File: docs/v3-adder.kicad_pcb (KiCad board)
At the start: 2 copper layers, 19.6 x 111.5 mm, 101 parts, among them J1 Thonkiconn, J2 Thonkiconn, J3 Thonkiconn, J4 Thonkiconn, J5 Thonkiconn, J6 Thonkiconn, J7 Thonkiconn, J8 Thonkiconn, P1 Eurorack 2x5, SW1 200-MSP3 (SPDT ON-OFF-ON), SW2 200-MSP3 (SPDT ON-OFF-ON), SW3 200-MSP3 (SPDT ON-OFF-ON), SW4 200-MSP3 (SPDT ON-OFF-ON), SW5 200-MSP1 (SPDT ON-ON), SW6 200-MDP6 (DPDT ON-ON-ON), SW7 200-MDP6 (DPDT ON-ON-ON), SW8 200-MDP6 (DPDT ON-ON-ON), U1 OPA4196, U2 OPA4196, U3 OPA4196, U4 L78L05, U5 L79L05

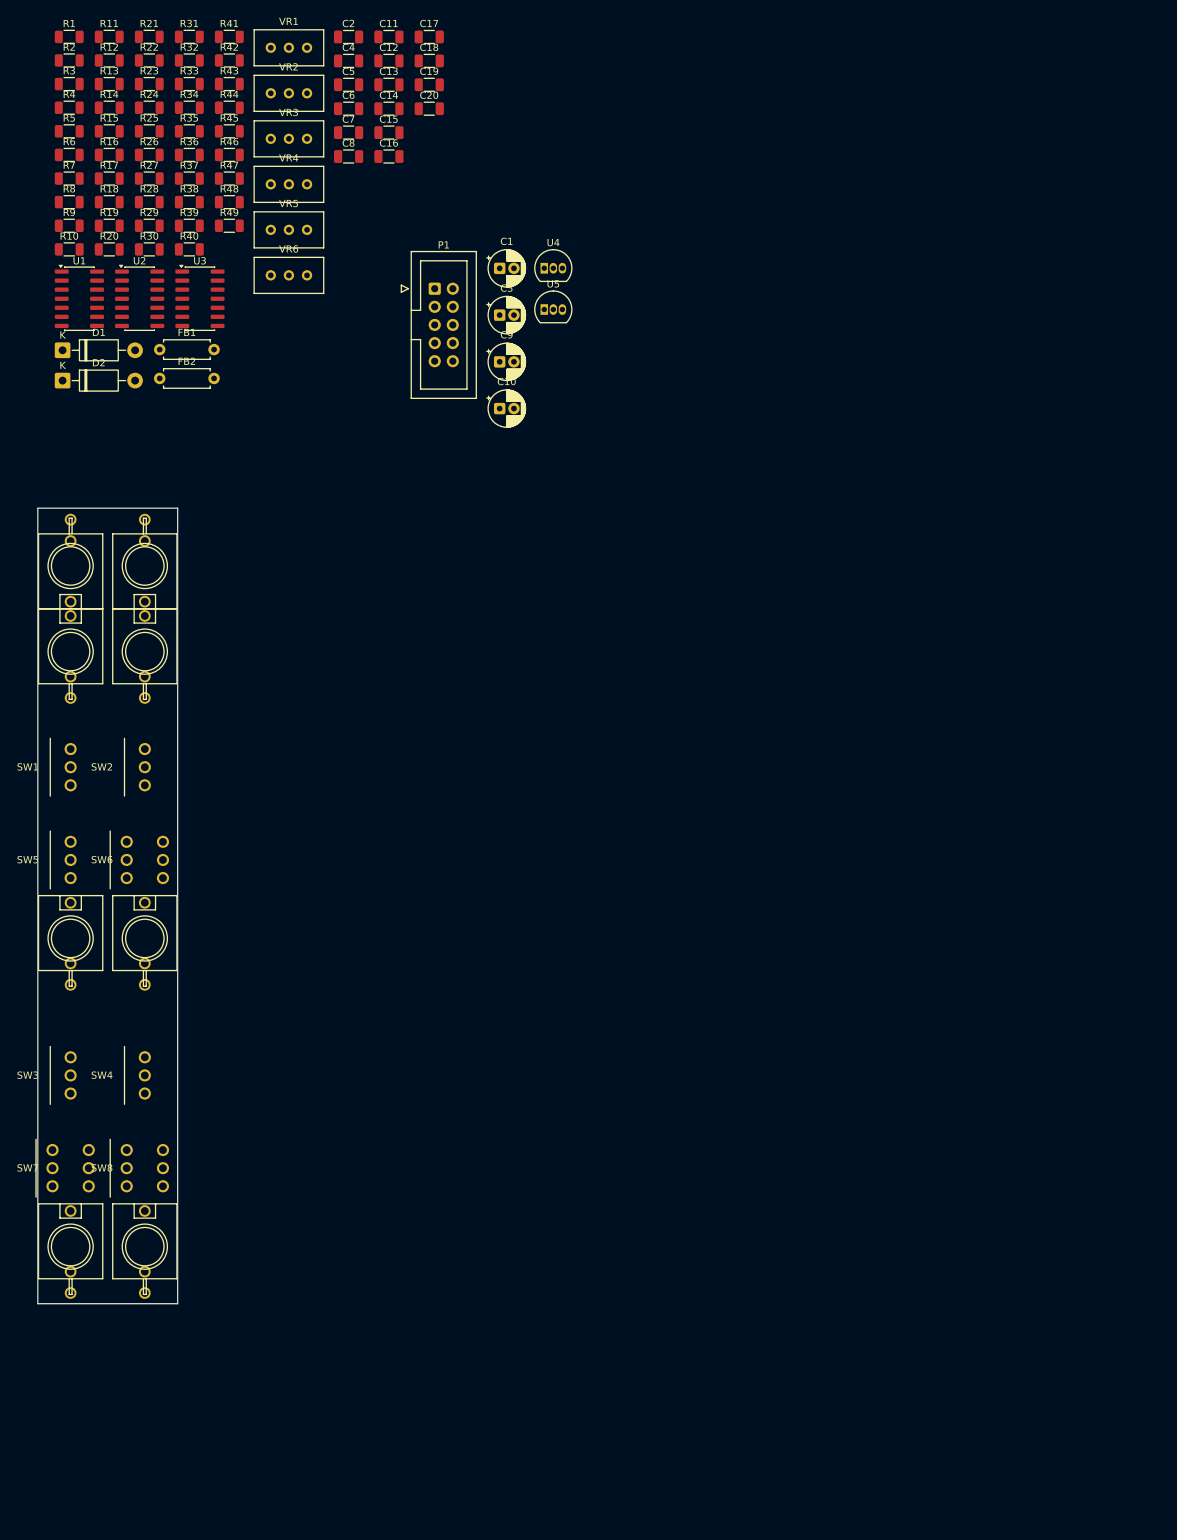
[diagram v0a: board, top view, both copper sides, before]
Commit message: Put component values on silk, and write them the same way in both files
Moves all 68 Fab-layer values to the matching silk layer, F.Fab -> F.SilkS
and B.Fab -> B.SilkS so back-side parts keep their mirrored justify. The 20
values that were already hidden stay hidden: "200-MDP6 (DPDT ON-ON-ON)" has
nowhere to go on a 19.6 mm board.

Trailing zeros that carry no information go with them -- 10.0k reads 10k,
1.00k reads 1k -- while 49.9k, 24.3k, 22.6k, 5.49k and 619R keep every
digit. Tolerance was never legible at 4 HP anyway; it lives in the BOM.

This turned out to be a consistency fix rather than a cosmetic one. The
schematic was the clean side: all ten 1k parts read 1.00k there and all
twenty 10k read 10.0k, but three of them had been edited to 1k in pcbnew,
and R8 disagreed outright (20.0k against the board's 20k). R31 read 1.00k
beside R32's 1k in the same ladder; R30 read 3.00k while R40, its exact
peer one stage along, read 3k. All 101 references now match between
schematic and board, with the netlist node-for-node identical to before
the edit and ERC still at zero.

gen_schematic.py moves in lockstep -- both the emitted values and the
check_function comparison strings, or --check would start failing. The E24
rationale comment keeps its decimals, since the argument turns on 3.01k
against 3.00k.

The BOM's "changes from what is currently in the schematic" table now reads
backwards for its first two rows, so it gets a note rather than a rewrite:
the parts did not change back, only the label got shorter.

Also carries the routing done in the meantime: 511 -> 677 segments, 98 more
vias, and no unconnected items left.
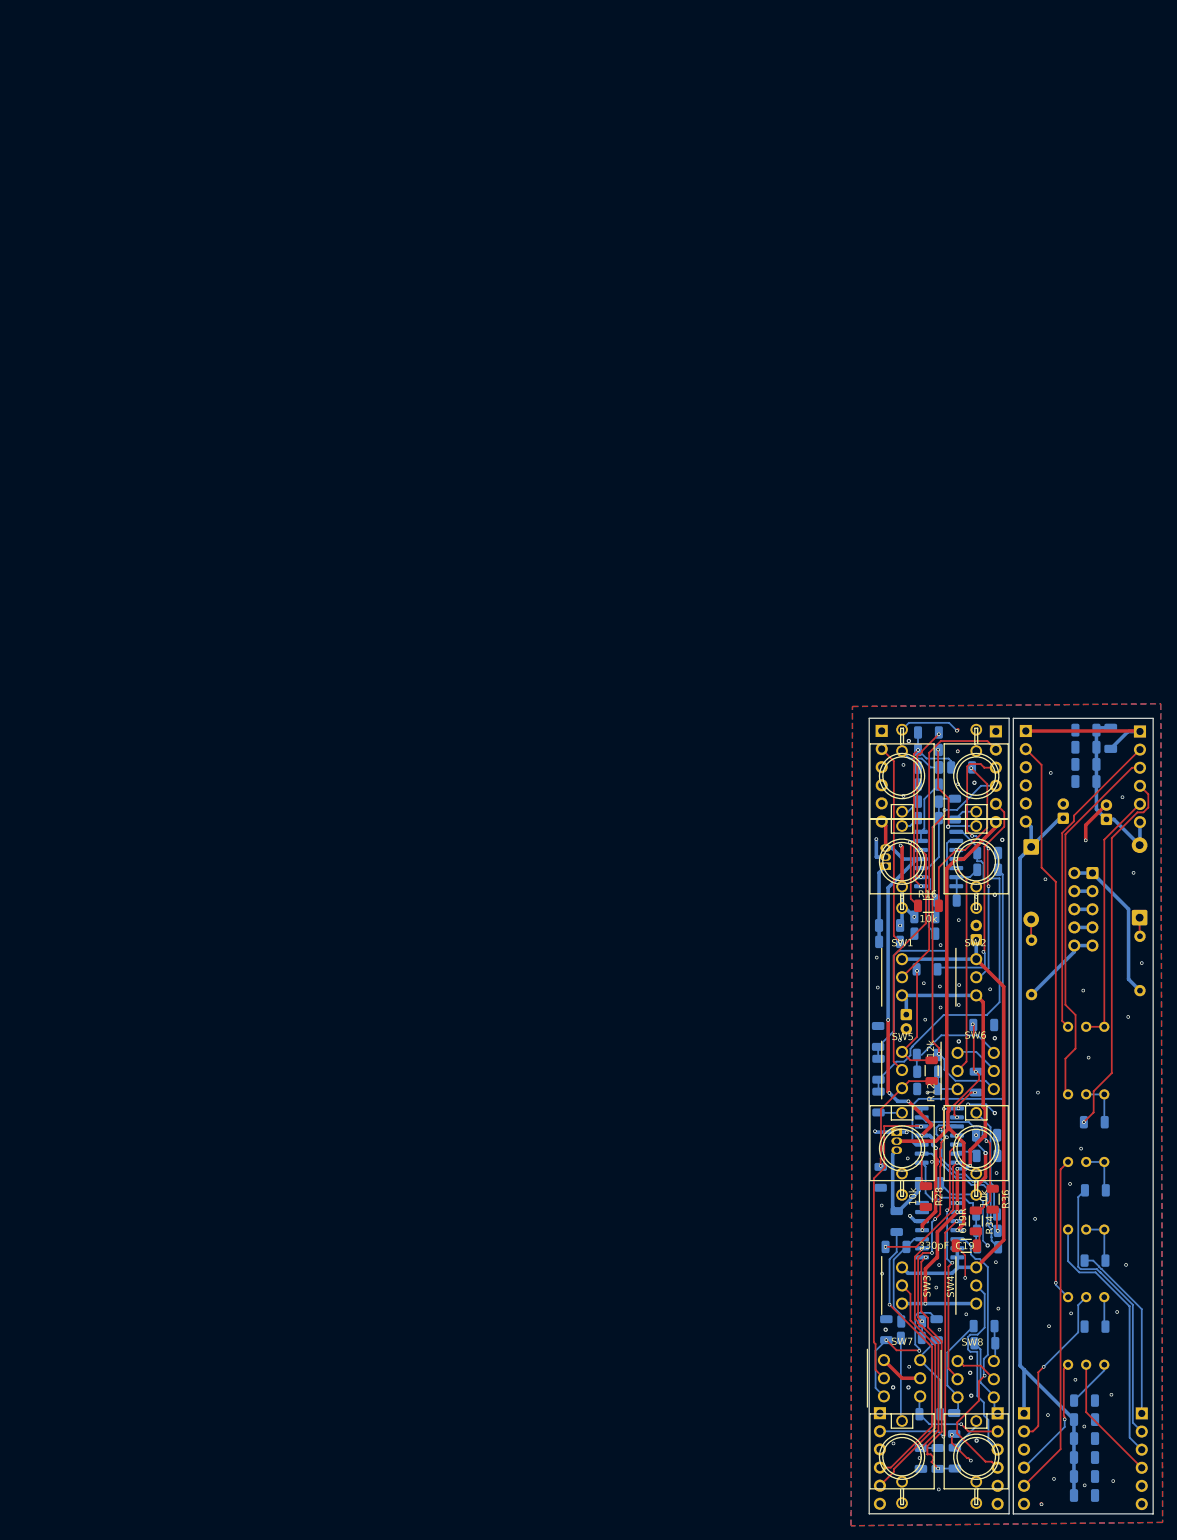
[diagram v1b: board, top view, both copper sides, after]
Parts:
- added REF**: PinHeader_1x06_P2.54mm_Vertical, Connector_PinHeader_2.54mm:PinHeader_1x06_P2.54mm_Vertical, B.Cu at (154.7, 39.8)
- added REF**: PinHeader_1x06_P2.54mm_Vertical, Connector_PinHeader_2.54mm:PinHeader_1x06_P2.54mm_Vertical, B.Cu at (118.5, 39.7)
- added REF**: PinHeader_1x06_P2.54mm_Vertical, Connector_PinHeader_2.54mm:PinHeader_1x06_P2.54mm_Vertical, B.Cu at (118.2, 135.3)
- added REF**: PinHeader_1x06_P2.54mm_Vertical, Connector_PinHeader_2.54mm:PinHeader_1x06_P2.54mm_Vertical, B.Cu at (154.9, 135.4)
- added REF**: PinHeader_1x06_P2.54mm_Vertical, Connector_PinHeader_2.54mm:PinHeader_1x06_P2.54mm_Vertical, B.Cu at (134.7, 135.4)
- added REF**: PinHeader_1x06_P2.54mm_Vertical, Connector_PinHeader_2.54mm:PinHeader_1x06_P2.54mm_Vertical, B.Cu at (134.5, 39.8)
- added REF**: PinHeader_1x06_P2.54mm_Vertical, Connector_PinHeader_2.54mm:PinHeader_1x06_P2.54mm_Vertical, B.Cu at (138.4, 135.4)
- added REF**: PinHeader_1x06_P2.54mm_Vertical, Connector_PinHeader_2.54mm:PinHeader_1x06_P2.54mm_Vertical, B.Cu at (138.7, 39.7)
- C1, C10, C11, C12, C13, C14, C15, C16, C17, C18, C2, C20, C3, C4, C5, C6, C7, C8, C9, D1, D2, FB1, FB2, P1, R1, R13, R14, R2, R23, R24, R3, R33, R4, R43, R44, U1, U2, U3, U4, U5, VR1, VR2, VR3, VR4, VR5, VR6: moved to B.Cu
- R10, R19, R21, R22, R29, R31, R32, R39, R41, R49: value 1.00k -> 1k; moved to B.Cu
- R11: value 12.0k -> 12k; moved to B.Cu
- R12: value 12.0k -> 12k
- R15, R17, R18, R25, R26, R27, R35, R37, R38, R45, R46, R47, R48, R5, R6, R7, R9: value 10.0k -> 10k; moved to B.Cu
- R16, R28, R36: value 10.0k -> 10k
- R20, R30, R40, R42: value 3.00k -> 3k; moved to B.Cu
- R8: value 20.0k -> 20k; moved to B.Cu
- moved R4 230.4 mm to (146.9, 133.6)
- moved R2 228.4 mm to (148.4, 123.2), turned to 180 degrees
- moved C5 223.0 mm to (146.9, 146.9)
- moved C2 221.9 mm to (146.9, 138.9)
- moved C11 216.9 mm to (146.9, 136.2)
- moved R32 216.3 mm to (125.2, 135.5), turned to 180 degrees
- moved C13 215.7 mm to (146.9, 141.6)
- moved C15 212.1 mm to (146.9, 144.2)
- moved R41 209.4 mm to (132.8, 123.1)
- moved R31 209.3 mm to (126.2, 123.6), turned to -90 degrees
- moved R42 208.7 mm to (132.9, 125.5), turned to 180 degrees
- moved R47 205.0 mm to (126.3, 141.7), turned to 90 degrees
- moved R43 204.7 mm to (148.4, 114.0)
- moved R48 201.0 mm to (124.0, 141.7), turned to -90 degrees
- moved R49 200.4 mm to (128.7, 141.6), turned to 90 degrees
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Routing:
- net /+12V: track 0.00 -> 179.7 mm, vias 0 -> 6
- net GND: track 0.00 -> 109.9 mm, vias 0 -> 88
- net /REFP_TOP: track 0.00 -> 107.4 mm, vias 0 -> 2
- net /S2_4th: track 0.00 -> 106.3 mm, vias 0 -> 3
- net /-12V: track 0.00 -> 93.8 mm, vias 0 -> 3
- net /LAD2_TOP: track 0.00 -> 87.7 mm, vias 0 -> 3
- net /LAD1_TOP: track 0.00 -> 87.3 mm
- net /LAD3_TOP: track 0.00 -> 81.1 mm
- net /VREF_N: track 0.00 -> 73.3 mm
- net /VREF_P: track 0.00 -> 71.9 mm, vias 0 -> 5
- net /LAD1_TRIM: track 0.00 -> 66.9 mm, vias 0 -> 1
- net /LAD4_TOP: track 0.00 -> 63.8 mm
- net /REFP_W: track 0.00 -> 63.3 mm, vias 0 -> 3
- net /REFN_W: track 0.00 -> 57.1 mm, vias 0 -> 1
- net /REFN_TOP: track 0.00 -> 56.9 mm, vias 0 -> 2
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- added copper zone on B.Cu, net GND
- added copper zone on F.Cu, net GND
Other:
- board size 19.6 x 111.5 mm -> 39.8 x 111.5 mm

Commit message: Sockets on the trimmer board, and give every footprint a 3D model path
The two cards' connectors were both on B.Cu, facing the same way, so they
could never have mated. Board B -- the one carrying VR1-VR6 -- now takes
PinSocket_1x06 on F.Cu, facing forward at board A's pins, which stay as
headers on A's rear. The cards stack by a plain 20.2 mm translation, one
board pitch, no flip.

Placed at rotation 0 rather than 180. A board footprint stores pad
coordinates with the rotation already baked in, while the library file
stores them unrotated, so instantiating the library body at rot 180 put the
pads in mirror order and broke every connection but pin 1. At rot 0 the
library coordinates are used as-is and land exactly where the old headers
were. All four pairs still agree pin for pin: 19 nets aligned to within
0.05 mm, 0 mismatches, 5 spare pins, and DRC back to 0 unconnected.

Models: SW_Taiway_200_SPDT had no (model) line at all, and the other two
custom footprints pointed at ${KIPRJMOD}/3d, which resolves to docs/3d --
a directory that does not exist, and the wrong place regardless for a
library shared across projects. They now resolve as
${KIPRJMOD}/../eurorack.3dshapes, mirroring how fp-lib-table already finds
eurorack.pretty. Board and library both updated, since the board caches its
own copy of every model path.

Every footprint now carries a model reference and 11 of 14 resolve. The
three that do not are vendor STEP files that are not on this machine and
cannot be generated; eurorack.3dshapes/README.md names them exactly and
flags that the SPDT filename is inferred from Taiway's scheme rather than
known.
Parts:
- removed the REF** at (154.7, 39.8)
- removed the REF** at (154.9, 135.4)
- removed the REF** at (138.4, 135.4)
- removed the REF** at (138.7, 39.7)
- added REF**: PinSocket_1x06_P2.54mm_Vertical, Connector_PinSocket_2.54mm:PinSocket_1x06_P2.54mm_Vertical, F.Cu at (154.7, 39.8)
- added REF**: PinSocket_1x06_P2.54mm_Vertical, Connector_PinSocket_2.54mm:PinSocket_1x06_P2.54mm_Vertical, F.Cu at (154.9, 135.4)
- added REF**: PinSocket_1x06_P2.54mm_Vertical, Connector_PinSocket_2.54mm:PinSocket_1x06_P2.54mm_Vertical, F.Cu at (138.4, 135.4)
- added REF**: PinSocket_1x06_P2.54mm_Vertical, Connector_PinSocket_2.54mm:PinSocket_1x06_P2.54mm_Vertical, F.Cu at (138.7, 39.7)

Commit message: Put the board-to-board connectors in the schematic
The eight interconnect footprints existed only on the board, carrying REF** and
absent from the schematic entirely. Update PCB from Schematic would have offered
to delete them, they were missing from the BOM, and nothing checked their pin
mapping -- it was correct, but only because it had been checked by hand.

Adds adder:HDR1x6 to the symbol library and eight instances: P2-P5 are the pin
headers on the control board's rear, P6-P9 the sockets on the trimmer board's
front, each Value naming the part it mates with. Board footprints annotated to
match. The five spare pins per side are carried as no-connects so they stay
available rather than becoming ERC noise.

Two things caught by checks rather than by care. Placing on a round 1 mm grid
put every pin off KiCad's 1.27 connection grid -- 46 warnings; coordinates are
now multiples of 1.27. Worse, the first placement dropped the row onto a wire at
y=344.17 and silently merged OUT4, S2_4th, REFN_TOP and REFN_W into one net.
ERC called it a naming conflict rather than a short, and the free-space check
that cleared the area had only looked at symbol and label anchors -- it never
read wire geometry, so it could not have seen the wire it collided with. The
placement now rasterises wires, symbols and labels together and asserts each
target box is clear before writing.

ERC 0 violations. DRC 0 errors, 0 unconnected. 109 references on both sides with
no orphans and no value or footprint mismatch. Netlist diff against the
pre-edit sheet: 48 connector pins added, 0 other nets changed.
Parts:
- P2: renamed from REF**; value PinHeader_1x06_P2.54mm_Vertical -> 1x6 pin header (mates P6)
- P3: renamed from REF**; value PinHeader_1x06_P2.54mm_Vertical -> 1x6 pin header (mates P7)
- P4: renamed from REF**; value PinHeader_1x06_P2.54mm_Vertical -> 1x6 pin header (mates P8)
- P5: renamed from REF**; value PinHeader_1x06_P2.54mm_Vertical -> 1x6 pin header (mates P9)
- P6: renamed from REF**; value PinSocket_1x06_P2.54mm_Vertical -> 1x6 socket (mates P2)
- P7: renamed from REF**; value PinSocket_1x06_P2.54mm_Vertical -> 1x6 socket (mates P3)
- P8: renamed from REF**; value PinSocket_1x06_P2.54mm_Vertical -> 1x6 socket (mates P4)
- P9: renamed from REF**; value PinSocket_1x06_P2.54mm_Vertical -> 1x6 socket (mates P5)

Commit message: Add v3 DigiKey BOM and reorganize references
Add an upload-ready DigiKey BOM (docs/BOM_v3_DigiKey.csv) and update README/docs to point v2.2 artifacts into a new reference/ directory. Adjust .gitignore for the local Numbers BOM, clarify C9/C10 mounting/ESR in docs/v3-BOM.md and reconcile sourcing notes. Move existing v2.2 files (schematic, gerbers, photos, BOM) into reference/, and update docs/v2.2-topology.md. Large kicad edits to docs/v3-adder.kicad_pcb and docs/v3-panel.kicad_pcb update silk, nets and layout metadata. These changes prepare sourcing and cleanly separate the finished v2.2 reference from v3 work.
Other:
- board text added: "ADDER V3 2026 MMM Control Board"
- board text added: "ADDER v3 Missing Mile Modular 2006 Trimmer Board"
